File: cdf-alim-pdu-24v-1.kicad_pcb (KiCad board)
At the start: 2 copper layers, 85 x 60 mm, 131 parts, among them J1 Conn_01x02, J10 Conn_01x02, J11 Conn_01x02, J12 Conn_01x02, J13 Conn_01x02, J14 Conn_01x02, J15 Conn_01x02, J16 Conn_01x02, J17 Conn_01x02, J2 Conn_01x02, J3 Conn_01x02, J4 Conn_01x02, J5 Conn_01x02, J6 Conn_01x02, J7 Conn_01x02, J8 Conn_01x02, J9 Conn_01x02, Q1 BSC019N04LS, Q2 BSC019N04LS, Q3 BSC019N04LS, U1 TPS25983, U2 TPS25983, U3 TPS25983, U4 HT753-1, U5 MX25947, U6 MX25947, U7 MX25947

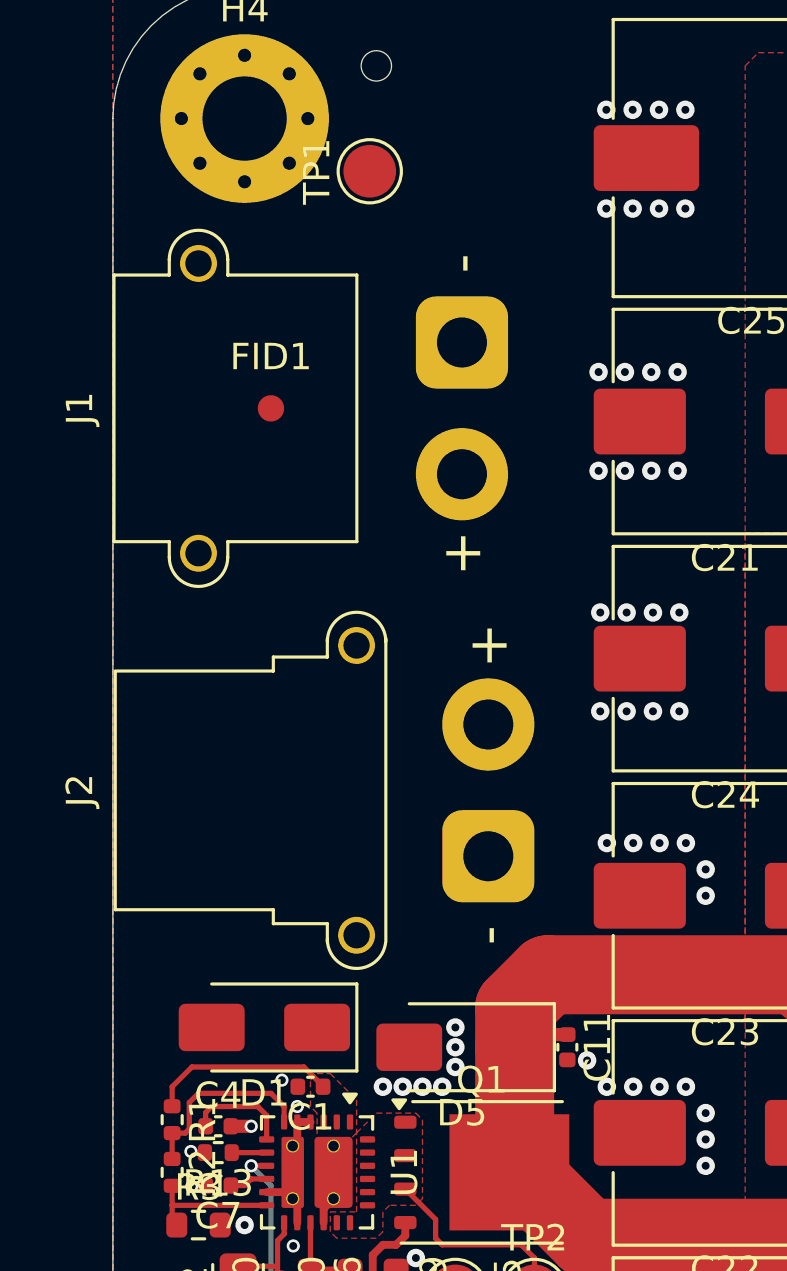
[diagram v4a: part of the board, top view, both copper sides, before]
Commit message: pcb: add +24v_in routing
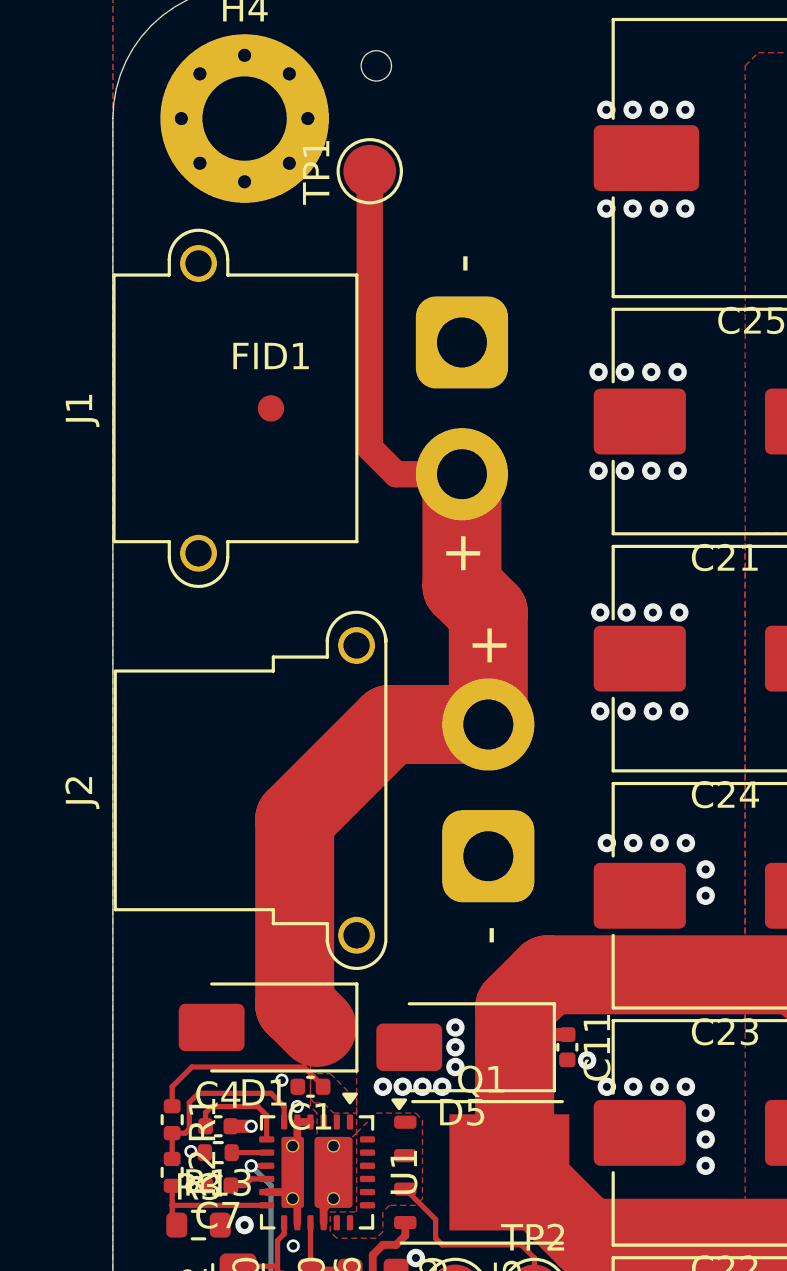
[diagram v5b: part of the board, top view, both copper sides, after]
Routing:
- net +24V_IN: track 8.17 -> 49.6 mm
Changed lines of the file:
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@@
 			(pinfunction "Pin_1_1")
 			(pintype "passive")
+			(thermal_bridge_width 2)
 		)
 		(pad "2" thru_hole circle
@@
 			(pinfunction "GND_26")
 			(pintype "passive")
+			(zone_connect 2)
 		)
 		(pad "26" smd roundrect
@@
 			(pinfunction "GND_26")
 			(pintype "passive")
+			(zone_connect 2)
 		)
 		(embedded_fonts no)
@@
 			(pinfunction "Pin_1_1")
 			(pintype "passive")
+			(thermal_bridge_width 2)
 		)
 		(pad "2" thru_hole circle
@@
 	)
 	(segment
+		(start 119.75 81)
+		(end 119.75 85.25)
+		(width 3)
+		(layer "F.Cu")
+		(net "+24V_IN")
+	)
+	(segment
+		(start 119.75 85.25)
+		(end 120.75 86.25)
+		(width 3)
+		(layer "F.Cu")
+		(net "+24V_IN")
+	)
+	(segment
 		(start 113.75 103.5)
 		(end 109.5 103.5)
@@
 	)
 	(segment
+		(start 120.75 90.5)
+		(end 117 90.5)
+		(width 3)
+		(layer "F.Cu")
+		(net "+24V_IN")
+	)
+	(segment
+		(start 116.25 80)
+		(end 116.25 69.5)
+		(width 1)
+		(layer "F.Cu")
+		(net "+24V_IN")
+	)
+	(segment
 		(start 114.5 108.875)
 		(end 114.875 108.5)
@@
 	)
 	(segment
+		(start 119.75 81)
+		(end 117.25 81)
+		(width 1)
+		(layer "F.Cu")
+		(net "+24V_IN")
+	)
+	(segment
 		(start 114.5 109.4125)
 		(end 114.5 108.875)
@@
 	)
 	(segment
+		(start 120.75 86.25)
+		(end 120.75 90.5)
+		(width 3)
+		(layer "F.Cu")
+		(net "+24V_IN")
+	)
+	(segment
+		(start 113.4 101.15)
+		(end 114.25 102)
+		(width 3)
+		(layer "F.Cu")
+		(net "+24V_IN")
+	)
+	(segment
+		(start 113.4 94.1)
+		(end 113.4 101.15)
+		(width 3)
+		(layer "F.Cu")
+		(net "+24V_IN")
+	)
+	(segment
 		(start 114.48 104.23)
 		(end 113.75 103.5)
@@
 	)
 	(segment
+		(start 117.25 81)
+		(end 116.25 80)
+		(width 1)
+		(layer "F.Cu")
+		(net "+24V_IN")
+	)
+	(segment
+		(start 117 90.5)
+		(end 113.4 94.1)
+		(width 3)
+		(layer "F.Cu")
+		(net "+24V_IN")
+	)
+	(segment
 		(start 150.5 97.25)
 		(end 148.9375 97.25)
@@
 			)
 		)
+	)
+	(zone
+		(net "+24V_IN")
+		(layer "F.Cu")
+		(hatch edge 0.5)
+		(priority 19)
+		(connect_pads yes
+			(clearance 0.2)
+		)
+		(min_thickness 0.15)
+		(fill yes
+			(thermal_gap 0.5)
+			(thermal_bridge_width 0.5)
+			(island_removal_mode 1)
+		)
+		(polygon
+			(pts
+				(xy 115.75 105.25) (xy 115.75 102) (xy 114 102) (xy 114 104.71) (xy 114.16 104.87) (xy 114.5 104.87)
+				(xy 114.88 105.25)
+			)
+		)

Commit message: pcb: add +3v3 leds routing
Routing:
- net +3V3: track 0.00 -> 86.4 mm, vias 0 -> 3
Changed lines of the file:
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@@
+	)
+	(segment
+		(start 115.5 118)
+		(end 115.5 116)
+		(width 0.3)
+		(layer "F.Cu")
+		(net "+3V3")
+	)
+	(segment
+		(start 116.05 118.55)
+		(end 115.5 118)
+		(width 0.3)
+		(layer "F.Cu")
+		(net "+3V3")
+	)
+	(segment
+		(start 121 120.75)
+		(end 123 120.75)
+		(width 0.3)
+		(layer "F.Cu")
+		(net "+3V3")
+	)
+	(segment
+		(start 120.5 118.25)
+		(end 119.3 118.25)
+		(width 0.3)
+		(layer "F.Cu")
+		(net "+3V3")
+	)
+	(segment
+		(start 117.55 118.25)
+		(end 117.25 118.55)
+		(width 0.3)
+		(layer "F.Cu")
+		(net "+3V3")
+	)
+	(segment
+		(start 121 118.75)
+		(end 120.5 118.25)
+		(width 0.3)
+		(layer "F.Cu")
+		(net "+3V3")
+	)
+	(segment
+		(start 115.5 116)
+		(end 112.75 113.25)
+		(width 0.3)
+		(layer "F.Cu")
+		(net "+3V3")
+	)
+	(segment
+		(start 112.75 113.25)
+		(end 112.75 112.51)
+		(width 0.3)
+		(layer "F.Cu")
+		(net "+3V3")
+	)
+	(segment
+		(start 143.5 75.25)
+		(end 143.5 74.26)
+		(width 0.3)
+		(layer "F.Cu")
+		(net "+3V3")
+	)
+	(segment
+		(start 119.3 118.25)
+		(end 117.55 118.25)
+		(width 0.3)
+		(layer "F.Cu")
+		(net "+3V3")
+	)
+	(segment
+		(start 117.25 118.55)
+		(end 116.05 118.55)
+		(width 0.3)
+		(layer "F.Cu")
+		(net "+3V3")
+	)
+	(segment
+		(start 121 120.75)
+		(end 121 118.75)
+		(width 0.3)
+		(layer "F.Cu")
+		(net "+3V3")
+	)
+	(segment
+		(start 143.5 121.75)
+		(end 143.5 121.01)
+		(width 0.3)
+		(layer "F.Cu")
+		(net "+3V3")
+	)
+	(via
+		(at 143.5 121.75)
+		(size 0.5)
+		(drill 0.3)
+		(layers "F.Cu" "B.Cu")
+		(net "+3V3")
+	)
+	(via
+		(at 143.5 75.25)
+		(size 0.5)
+		(drill 0.3)
+		(layers "F.Cu" "B.Cu")
+		(net "+3V3")
+	)
+	(via
+		(at 123 120.75)
+		(size 0.5)
+		(drill 0.3)
+		(layers "F.Cu" "B.Cu")
+		(net "+3V3")
+	)
+	(segment
+		(start 141.25 121.75)
+		(end 143.5 121.75)
+		(width 0.3)
+		(layer "B.Cu")
+		(net "+3V3")
+	)
+	(segment
+		(start 139.5 120)
+		(end 139.5 79.25)
+		(width 0.3)
+		(layer "B.Cu")
+		(net "+3V3")
+	)
+	(segment
+		(start 123 120.75)
+		(end 123.75 120)
+		(width 0.3)
+		(layer "B.Cu")
+		(net "+3V3")
+	)
+	(segment
+		(start 123.75 120)
+		(end 139.5 120)
+		(width 0.3)
+		(layer "B.Cu")
+		(net "+3V3")
+	)
+	(segment
+		(start 139.5 120)
+		(end 141.25 121.75)
+		(width 0.3)
+		(layer "B.Cu")
+		(net "+3V3")
+	)
+	(segment
+		(start 139.5 79.25)
+		(end 143.5 75.25)
+		(width 0.3)
+		(layer "B.Cu")
+		(net "+3V3")
 	)
 	(segment

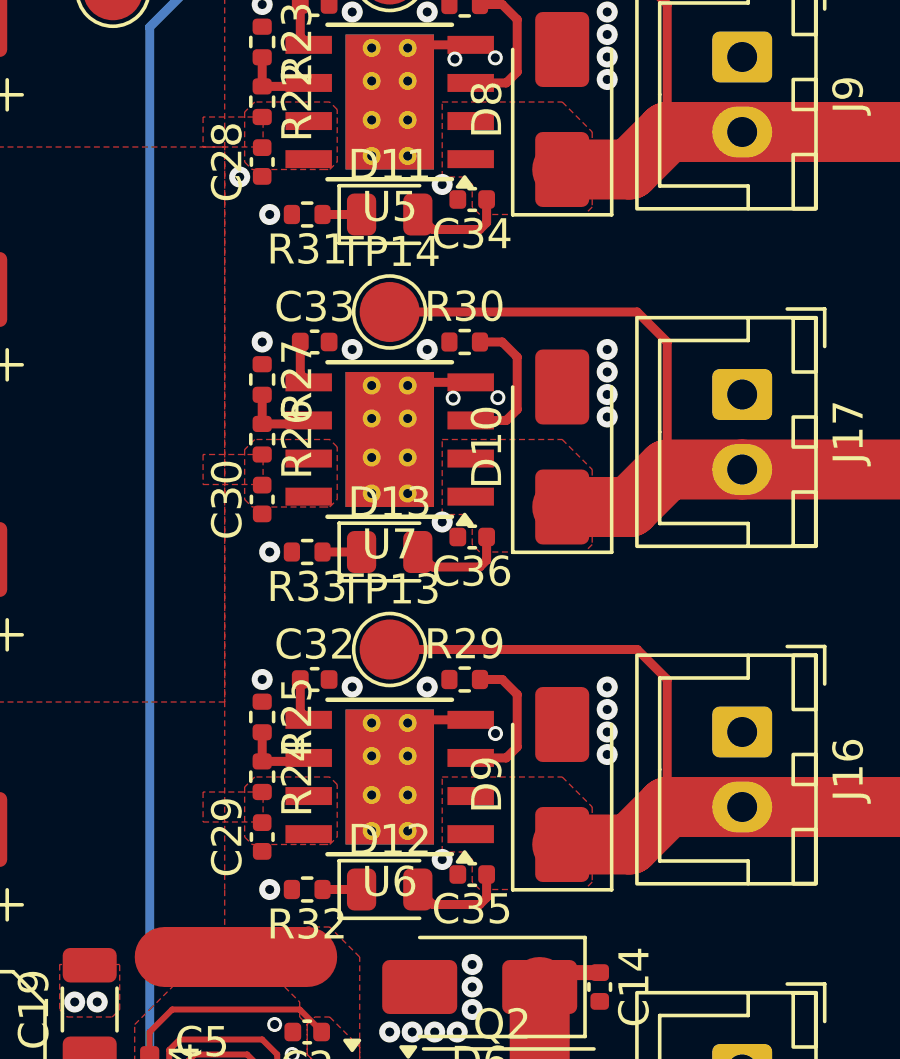
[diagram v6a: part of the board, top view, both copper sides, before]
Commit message: pcb: add missing connections
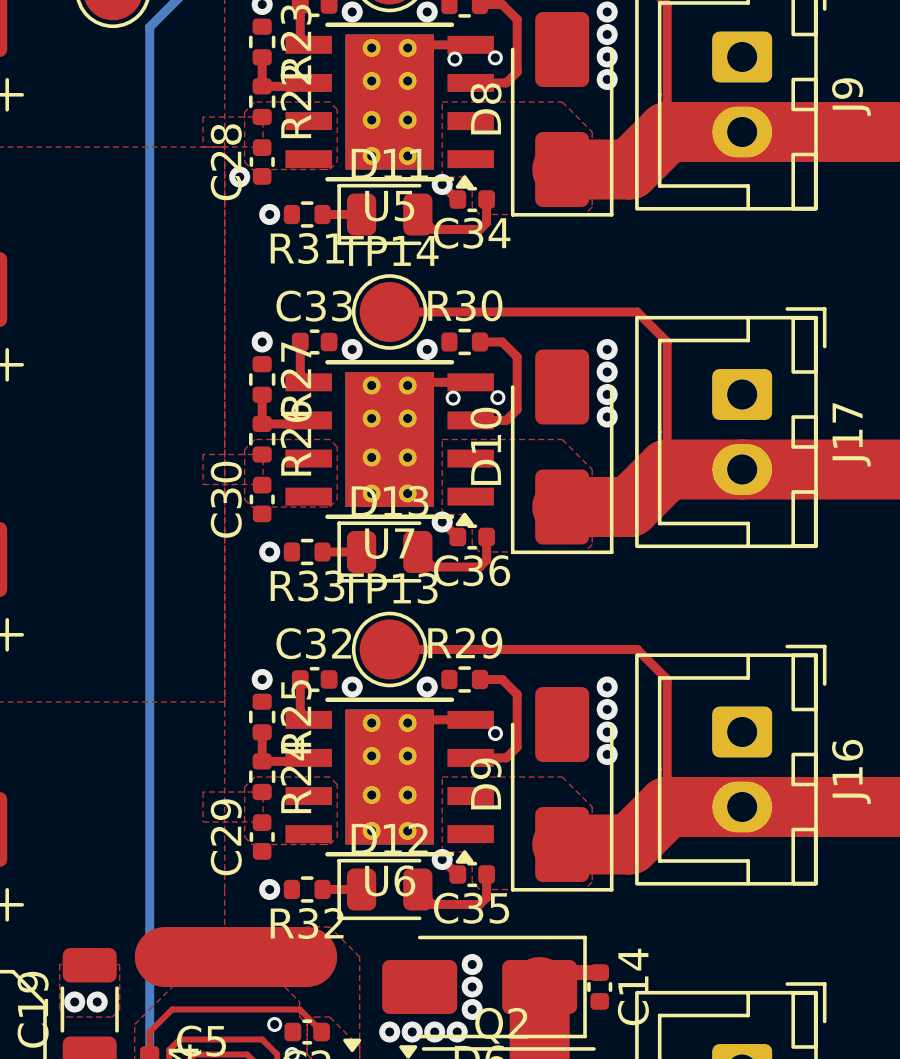
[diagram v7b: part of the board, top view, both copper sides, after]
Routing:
- net GND: track 19.2 -> 21.4 mm
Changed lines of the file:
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@@
+	)
+	(segment
+		(start 149.75 107.5)
+		(end 149.25 107)
+		(width 0.3)
+		(layer "F.Cu")
+		(net "GND")
 	)
 	(segment
@@
 	)
 	(segment
+		(start 149.77 96.25)
+		(end 149.75 96.25)
+		(width 0.3)
+		(layer "F.Cu")
+		(net "GND")
+	)
+	(segment
 		(start 144.75 67.3375)
 		(end 144.25 67.3375)
+		(width 0.3)
+		(layer "F.Cu")
+		(net "GND")
+	)
+	(segment
+		(start 149.75 85)
+		(end 149.25 84.5)
 		(width 0.3)
 		(layer "F.Cu")
@@
 	)
 	(segment
+		(start 149.75 96.25)
+		(end 149.25 95.75)
+		(width 0.3)
+		(layer "F.Cu")
+		(net "GND")
+	)
+	(segment
 		(start 143.0875 70)
 		(end 143.75 70)
@@
 	)
 	(segment
+		(start 149.77 85)
+		(end 149.75 85)
+		(width 0.3)
+		(layer "F.Cu")
+		(net "GND")
+	)
+	(segment
 		(start 143.0875 116.75)
 		(end 143.75 116.75)
 		(width 0.3)
 		(layer "F.Cu")
+		(net "GND")
+	)
+	(segment
+		(start 149.77 107.5)
+		(end 149.75 107.5)
+		(width 0.3)
+		(layer "F.Cu")
